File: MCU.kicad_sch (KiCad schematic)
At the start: 4 parts, among them U2 BL652

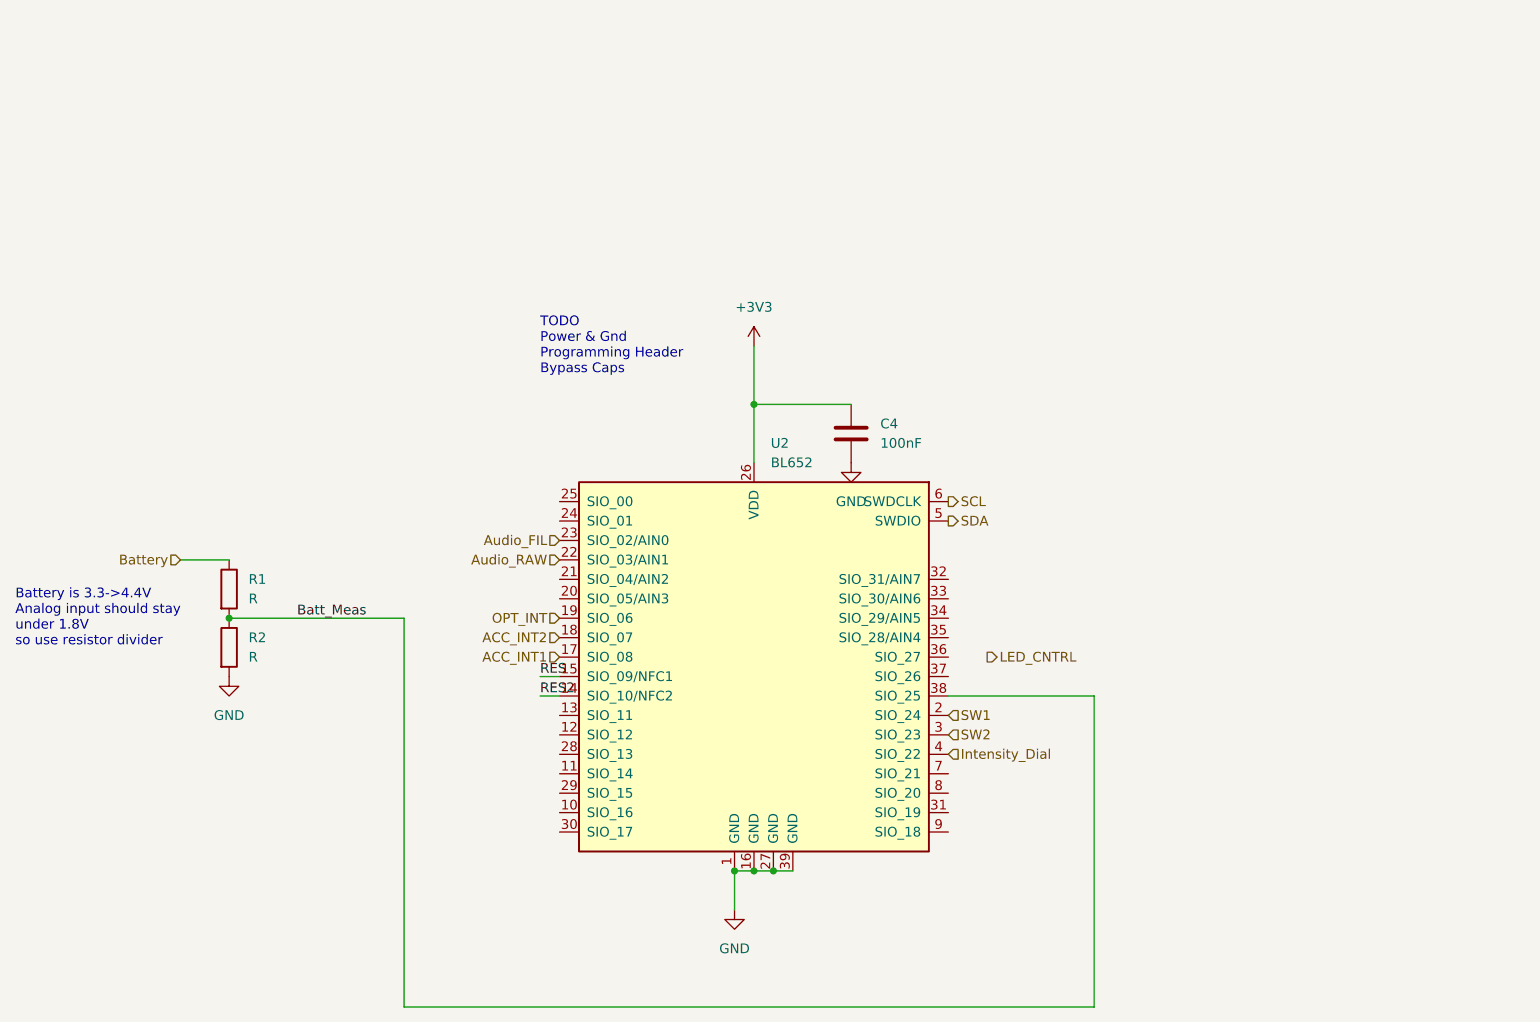
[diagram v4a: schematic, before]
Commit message: pcB rev2
need to fix reference texts on PCB, figure out MEMs mic wiring
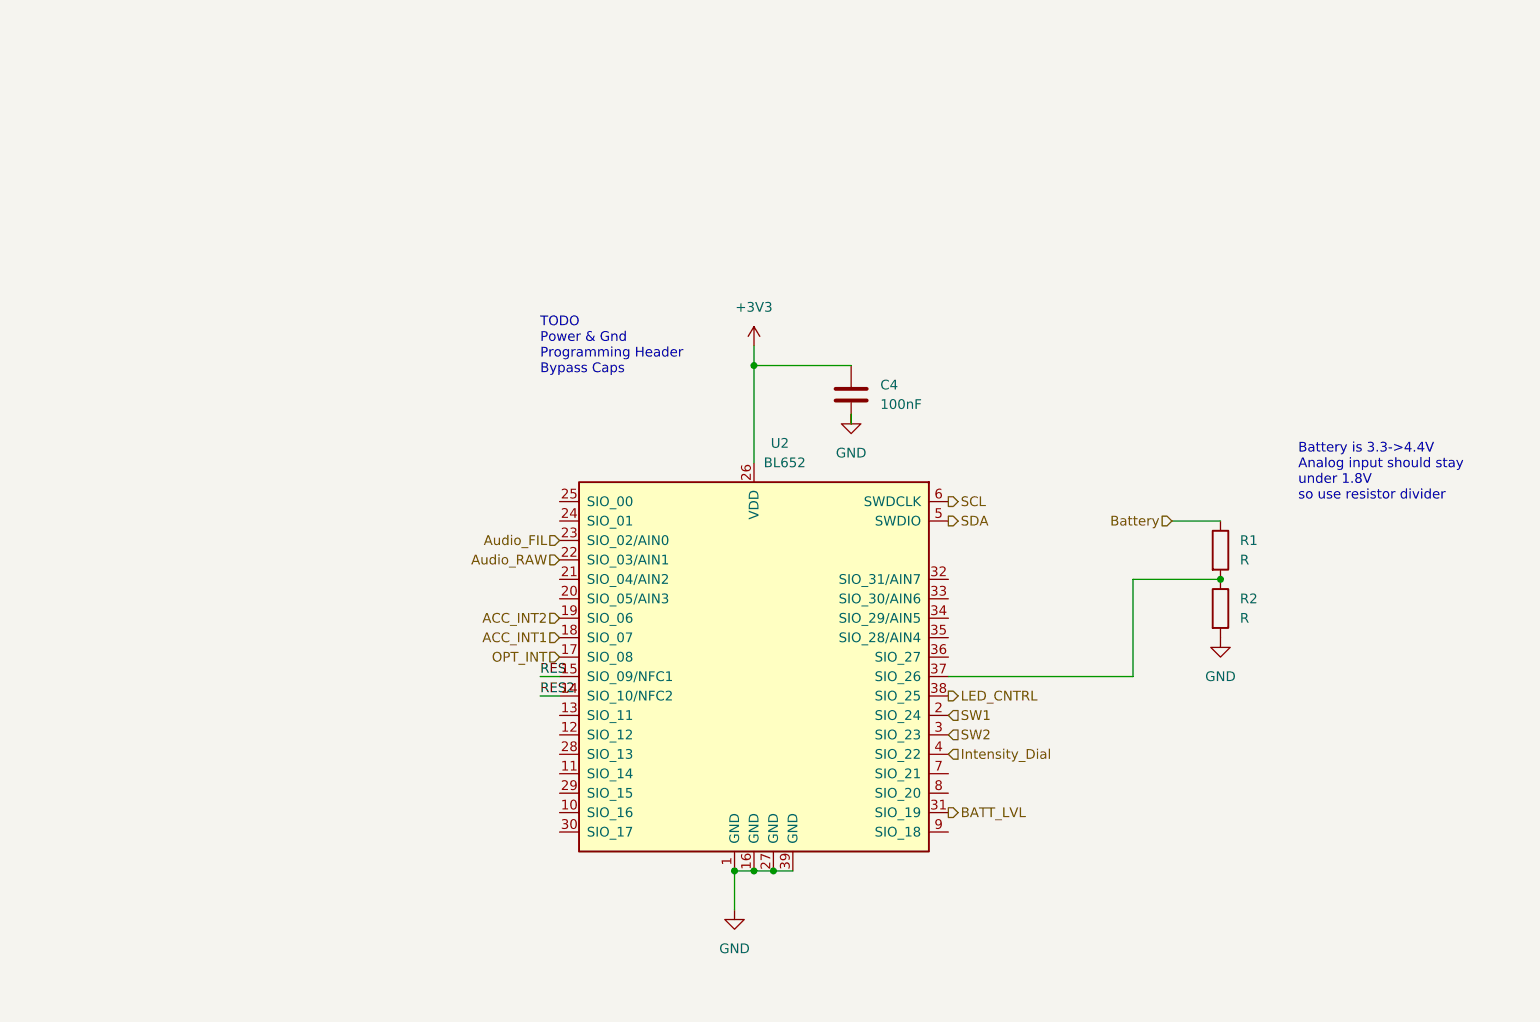
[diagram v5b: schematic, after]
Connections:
- net ACC_INT1: now also U2.18 (SIO_07); no longer U2.17 (SIO_08)
- net ACC_INT2: now also U2.19 (SIO_06); no longer U2.18 (SIO_07)
- net LED_CNTRL: now also U2.38 (SIO_25)
- net OPT_INT: now also U2.17 (SIO_08); no longer U2.19 (SIO_06)
- net BATT_LVL: now reaches U2.31 (SIO_19)
- net at U2.37 (SIO_26): now also R1.2, R2.1
- removed net Batt_Meas: R1.2, R2.1, U2.38 (SIO_25)
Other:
- moved on the sheet: C4, R1, R2

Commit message: new pcb rev with updated audio filter
The only ERC and DRC warnings/errors are unconnected pins and silkscreen text issues. There are two DRC issues that have to do with the mic, but I don't think they're an issue
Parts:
- added D2: LED_RBAG, symbol Device:LED_RBAG
- added R5 (x3): 100R, Resistor_SMD:R_0603_1608Metric_Pad0.98x0.95mm_HandSolder, symbol Device:R
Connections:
- net +3V3: now also D2.3 (A)
- net ACC_INT1: now also U2.20 (SIO_05/AIN3); no longer U2.18 (SIO_07)
- net ACC_INT2: now also U2.21 (SIO_04/AIN2); no longer U2.19 (SIO_06)
- net Audio_FIL: now also U2.29 (SIO_15); no longer U2.23 (SIO_02/AIN0)
- net Audio_RAW: now also U2.28 (SIO_13); no longer U2.22 (SIO_03/AIN1)
- net SCL: now also U2.19 (SIO_06); no longer U2.6 (SWDCLK)
- net SDA: now also U2.18 (SIO_07); no longer U2.5 (SWDIO)
- net at R1.2, R2.1: now also U2.32 (SIO_31/AIN7); no longer U2.37 (SIO_26)
- net at U2.11 (SIO_14): now also R5.2
- net at U2.12 (SIO_12): now also R5.2
- net at U2.13 (SIO_11): now also R5.1
- net BATT_LVL: no longer names the net of U2.31 (SIO_19)
- new net: D2.1 (RK), R5.1
- new net: D2.2 (BK), R5.2
- new net: D2.4 (GK), R5.1
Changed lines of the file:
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@@
+    (stroke (width 0) (type default))
+  )
+  (wire (pts (xy 71.12 119.38) (xy 76.2 119.38))
     (stroke (width 0) (type default))
   )
@@
     (stroke (width 0) (type default))
   )
+  (wire (pts (xy 83.82 119.38) (xy 83.82 115.57))
+    (stroke (width 0) (type default))
+  )
+  (wire (pts (xy 60.96 114.3) (xy 57.15 114.3))
+    (stroke (width 0) (type default))
+  )
+  (wire (pts (xy 83.82 107.95) (xy 104.14 107.95))
+    (stroke (width 0) (type default))
+  )
   (wire (pts (xy 142.24 68.58) (xy 142.24 69.85))
     (stroke (width 0) (type default))
   )
-  (wire (pts (xy 101.6 102.87) (xy 104.14 102.87))
-    (stroke (width 0) (type default))
-  )
-  (wire (pts (xy 101.6 105.41) (xy 104.14 105.41))
-    (stroke (width 0) (type default))
-  )
-  (wire (pts (xy 179.07 90.17) (xy 179.07 102.87))
+  (wire (pts (xy 87.63 102.87) (xy 104.14 102.87))
+    (stroke (width 0) (type default))
+  )
+  (wire (pts (xy 71.12 107.95) (xy 76.2 107.95))
+    (stroke (width 0) (type default))
+  )
+  (wire (pts (xy 71.12 109.22) (xy 71.12 107.95))
+    (stroke (width 0) (type default))
+  )
+  (wire (pts (xy 57.15 111.76) (xy 57.15 114.3))
+    (stroke (width 0) (type default))
+  )
+  (wire (pts (xy 87.63 105.41) (xy 104.14 105.41))
+    (stroke (width 0) (type default))
+  )
+  (wire (pts (xy 83.82 110.49) (xy 104.14 110.49))
+    (stroke (width 0) (type default))
+  )
+  (wire (pts (xy 71.12 114.3) (xy 71.12 110.49))
+    (stroke (width 0) (type default))
+  )
+  (wire (pts (xy 83.82 115.57) (xy 104.14 115.57))
     (stroke (width 0) (type default))
   )
@@
     (stroke (width 0) (type default))
   )
-  (wire (pts (xy 190.5 90.17) (xy 179.07 90.17))
+  (wire (pts (xy 154.94 90.17) (xy 190.5 90.17))
     (stroke (width 0) (type default))
   )
@@
     (stroke (width 0) (type default))
   )
-  (wire (pts (xy 179.07 102.87) (xy 154.94 102.87))
+  (wire (pts (xy 71.12 110.49) (xy 76.2 110.49))
     (stroke (width 0) (type default))
   )
@@
     (effects (font (size 1.27 1.27)) (justify left bottom))
   )
-  (label "RES2" (at 101.6 105.41 0) (fields_autoplaced)
+  (label "RES2" (at 87.63 105.41 0) (fields_autoplaced)
     (effects (font (size 1.27 1.27)) (justify left bottom))
   )
-  (label "RES" (at 101.6 102.87 0) (fields_autoplaced)
+  (label "RES" (at 87.63 102.87 0) (fields_autoplaced)
     (effects (font (size 1.27 1.27)) (justify left bottom))
   )
@@
     (effects (font (size 1.27 1.27)) (justify left))
   )
-  (hierarchical_label "Audio_RAW" (shape input) (at 104.14 87.63 180) (fields_autoplaced)
+  (hierarchical_label "Audio_RAW" (shape input) (at 104.14 113.03 180) (fields_autoplaced)
     (effects (font (size 1.27 1.27)) (justify right))
   )
@@
     (effects (font (size 1.27 1.27)) (justify right))
   )
-  (hierarchical_label "SDA" (shape output) (at 154.94 82.55 0) (fields_autoplaced)
-    (effects (font (size 1.27 1.27)) (justify left))
-  )
-  (hierarchical_label "BATT_LVL" (shape output) (at 154.94 120.65 0) (fields_autoplaced)
-    (effects (font (size 1.27 1.27)) (justify left))
-  )
-  (hierarchical_label "ACC_INT1" (shape input) (at 104.14 97.79 180) (fields_autoplaced)
-    (effects (font (size 1.27 1.27)) (justify right))
-  )
-  (hierarchical_label "ACC_INT2" (shape input) (at 104.14 95.25 180) (fields_autoplaced)
+  (hierarchical_label "SDA" (shape output) (at 104.14 97.79 180) (fields_autoplaced)
+    (effects (font (size 1.27 1.27)) (justify right))
+  )
+  (hierarchical_label "ACC_INT1" (shape input) (at 104.14 92.71 180) (fields_autoplaced)
+    (effects (font (size 1.27 1.27)) (justify right))
+  )
+  (hierarchical_label "ACC_INT2" (shape input) (at 104.14 90.17 180) (fields_autoplaced)
     (effects (font (size 1.27 1.27)) (justify right))
   )
@@
     (effects (font (size 1.27 1.27)) (justify left))
   )
-  (hierarchical_label "Audio_FIL" (shape input) (at 104.14 85.09 180) (fields_autoplaced)
-    (effects (font (size 1.27 1.27)) (justify right))
-  )
-  (hierarchical_label "SCL" (shape output) (at 154.94 80.01 0) (fields_autoplaced)
-    (effects (font (size 1.27 1.27)) (justify left))
+  (hierarchical_label "Audio_FIL" (shape input) (at 104.14 118.11 180) (fields_autoplaced)
+    (effects (font (size 1.27 1.27)) (justify right))
+  )
+  (hierarchical_label "SCL" (shape output) (at 104.14 95.25 180) (fields_autoplaced)
+    (effects (font (size 1.27 1.27)) (justify right))
   )
   (hierarchical_label "Intensity_Dial" (shape input) (at 154.94 113.03 0) (fields_autoplaced)
@@
     )
   )
+  (symbol (lib_id "Device:LED_RBAG") (at 66.04 114.3 180) (unit 1)
+    (in_bom yes) (on_board yes) (dnp no) (fields_autoplaced)
+    (property "Reference" "D2" (at 66.04 101.6 0)
+      (effects (font (size 1.27 1.27)))
+    )
+    (property "Value" "LED_RBAG" (at 66.04 104.14 0)
+      (effects (font (size 1.27 1.27)))
+    )
+    (property "Footprint" "" (at 66.04 113.03 0)
+      (effects (font (size 1.27 1.27)) hide)
+    )
+    (property "Datasheet" "~" (at 66.04 113.03 0)
+      (effects (font (size 1.27 1.27)) hide)
+    )
+    (pin "1")
+    (pin "2")
+    (pin "3")
+    (pin "4")
+    (instances
+      (project "VibeLight"
+        (path "/704dec10-a4c2-4298-be85-193d9407f59f/a98cecf9-ef60-4d48-8d8f-6fc42778f104"
+          (reference "D2") (unit 1)
+        )
+      )
+    )
+  )
+  (symbol (lib_id "Device:R") (at 80.01 119.38 90) (unit 1)
+    (in_bom yes) (on_board yes) (dnp no) (fields_autoplaced)
+    (property "Reference" "R5" (at 80.01 125.73 90)
+      (effects (font (size 1.27 1.27)))
+    )
+    (property "Value" "100R" (at 80.01 123.19 90)
+      (effects (font (size 1.27 1.27)))
+    )
+    (property "Footprint" "Resistor_SMD:R_0603_1608Metric_Pad0.98x0.95mm_HandSolder" (at 80.01 121.158 90)
+      (effects (font (size 1.27 1.27)) hide)
+    )
+    (property "Datasheet" "~" (at 80.01 119.38 0)
+      (effects (font (size 1.27 1.27)) hide)
+    )
+    (pin "1")
+    (pin "2")
+    (instances
+      (project "VibeLight"
+        (path "/704dec10-a4c2-4298-be85-193d9407f59f"
+          (reference "R5") (unit 1)
+        )
+        (path "/704dec10-a4c2-4298-be85-193d9407f59f/a98cecf9-ef60-4d48-8d8f-6fc42778f104"
+          (reference "R5") (unit 1)
+        )
+      )
+    )
+  )
   (symbol (lib_id "power:GND") (at 190.5 97.79 0) (unit 1)
     (in_bom yes) (on_board yes) (dnp no) (fields_autoplaced)
@@
         (path "/704dec10-a4c2-4298-be85-193d9407f59f/a98cecf9-ef60-4d48-8d8f-6fc42778f104"
           (reference "#PWR017") (unit 1)
+        )
+      )
+    )
+  )
+  (symbol (lib_id "power:+3V3") (at 57.15 111.76 0) (unit 1)
+    (in_bom yes) (on_board yes) (dnp no) (fields_autoplaced)
+    (property "Reference" "#PWR037" (at 57.15 115.57 0)
+      (effects (font (size 1.27 1.27)) hide)
+    )
+    (property "Value" "+3V3" (at 57.15 106.68 0)
+      (effects (font (size 1.27 1.27)))
+    )
+    (property "Footprint" "" (at 57.15 111.76 0)
+      (effects (font (size 1.27 1.27)) hide)
+    )
+    (property "Datasheet" "" (at 57.15 111.76 0)
+      (effects (font (size 1.27 1.27)) hide)
+    )
+    (pin "1")
+    (instances
+      (project "VibeLight"
+        (path "/704dec10-a4c2-4298-be85-193d9407f59f/a98cecf9-ef60-4d48-8d8f-6fc42778f104"
+          (reference "#PWR037") (unit 1)
+        )
+      )
+    )
+  )
+  (symbol (lib_id "Device:R") (at 80.01 110.49 90) (unit 1)
+    (in_bom yes) (on_board yes) (dnp no) (fields_autoplaced)
+    (property "Reference" "R5" (at 80.01 116.84 90)
+      (effects (font (size 1.27 1.27)))
+    )
+    (property "Value" "100R" (at 80.01 114.3 90)
+      (effects (font (size 1.27 1.27)))
+    )
+    (property "Footprint" "Resistor_SMD:R_0603_1608Metric_Pad0.98x0.95mm_HandSolder" (at 80.01 112.268 90)
+      (effects (font (size 1.27 1.27)) hide)
+    )
+    (property "Datasheet" "~" (at 80.01 110.49 0)
+      (effects (font (size 1.27 1.27)) hide)
+    )
+    (pin "1")
+    (pin "2")
+    (instances
+      (project "VibeLight"
+        (path "/704dec10-a4c2-4298-be85-193d9407f59f"
+          (reference "R5") (unit 1)
+        )
+        (path "/704dec10-a4c2-4298-be85-193d9407f59f/a98cecf9-ef60-4d48-8d8f-6fc42778f104"
+          (reference "R6") (unit 1)
+        )
+      )
+    )
+  )
+  (symbol (lib_id "Device:R") (at 80.01 107.95 270) (unit 1)
+    (in_bom yes) (on_board yes) (dnp no) (fields_autoplaced)
+    (property "Reference" "R5" (at 80.01 101.6 90)
+      (effects (font (size 1.27 1.27)))
+    )
+    (property "Value" "100R" (at 80.01 104.14 90)
+      (effects (font (size 1.27 1.27)))
+    )
+    (property "Footprint" "Resistor_SMD:R_0603_1608Metric_Pad0.98x0.95mm_HandSolder" (at 80.01 106.172 90)
+      (effects (font (size 1.27 1.27)) hide)
+    )
+    (property "Datasheet" "~" (at 80.01 107.95 0)
+      (effects (font (size 1.27 1.27)) hide)
+    )
+    (pin "1")
+    (pin "2")
+    (instances
+      (project "VibeLight"
+        (path "/704dec10-a4c2-4298-be85-193d9407f59f"
+          (reference "R5") (unit 1)
+        )
+        (path "/704dec10-a4c2-4298-be85-193d9407f59f/a98cecf9-ef60-4d48-8d8f-6fc42778f104"
+          (reference "R7") (unit 1)
         )
       )
@@
         )
         (path "/704dec10-a4c2-4298-be85-193d9407f59f/a98cecf9-ef60-4d48-8d8f-6fc42778f104"
-          (reference "U3") (unit 1)
-        )
-      )
+          (reference "MCU1") (unit 1)
+        )
+      )
